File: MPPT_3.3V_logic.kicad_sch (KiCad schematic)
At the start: 28 parts, among them Q1 PMOS, Q11 PMOS, Q2 PMOS, U1 LTC4412xS6, U16 TPS259470ARPWR, U2 TPS62177DQCR, U3 LTC4412xS6, U5 LTC2965HDD-PBF

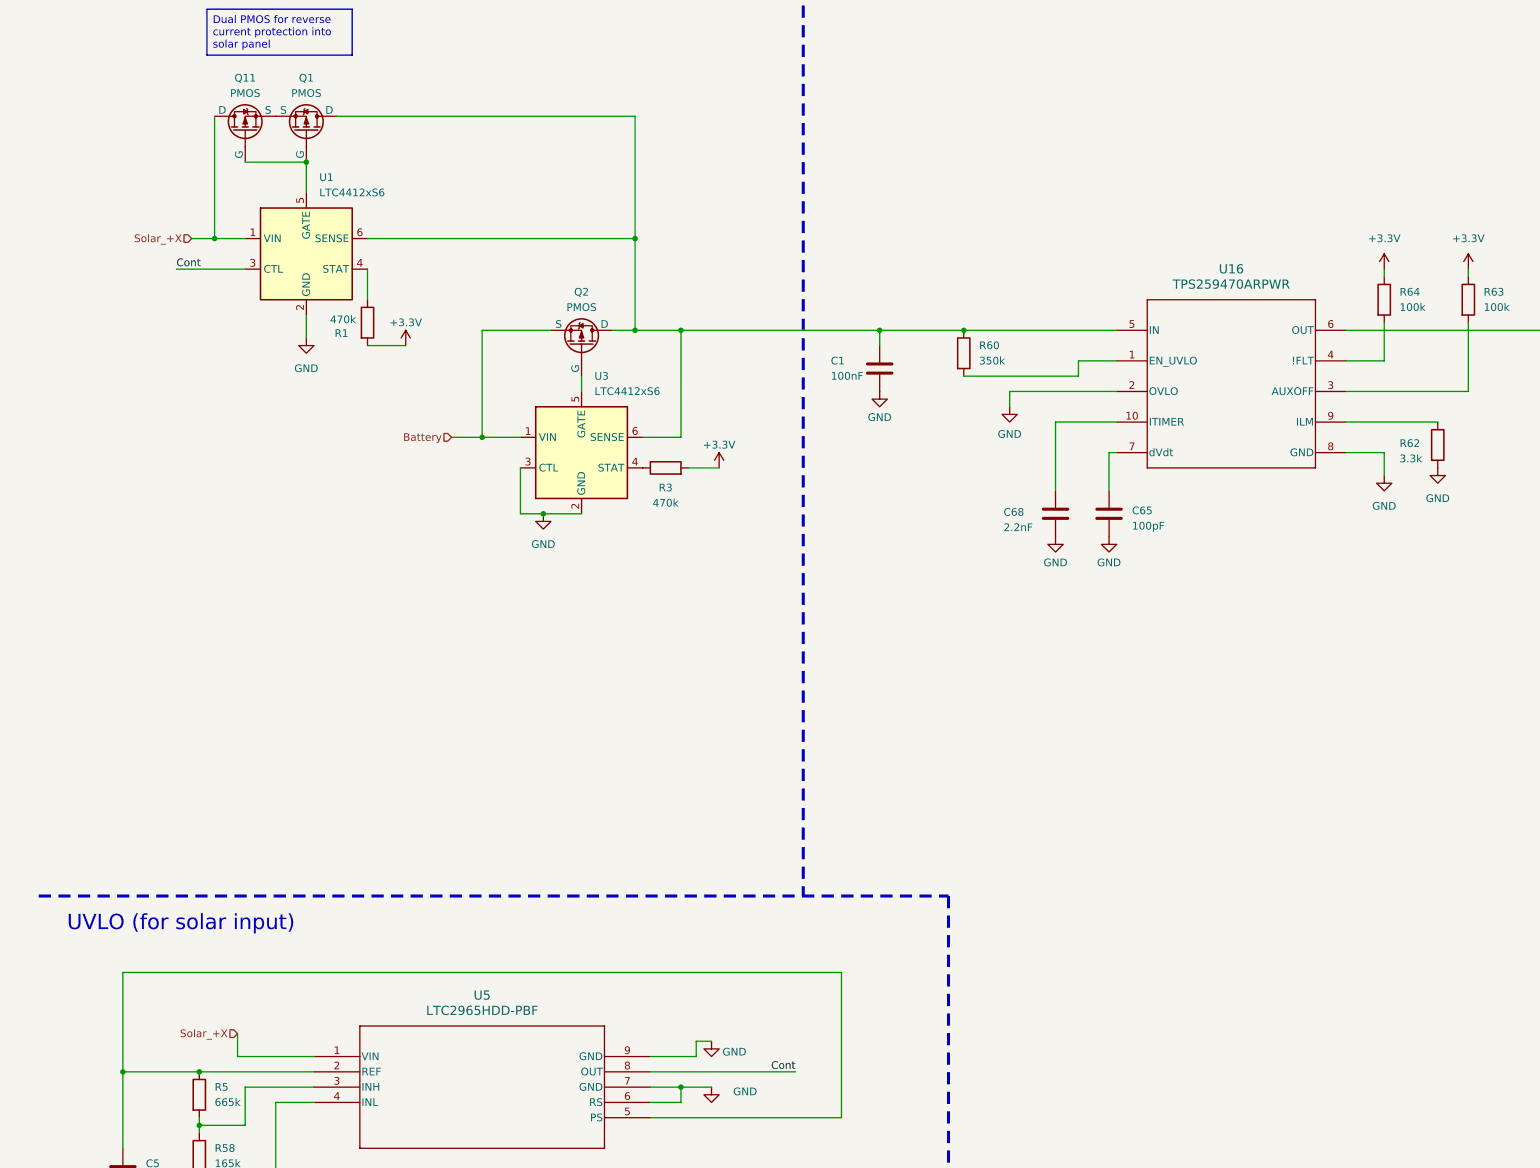
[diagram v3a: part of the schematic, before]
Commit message: added current sensing and e-fuses
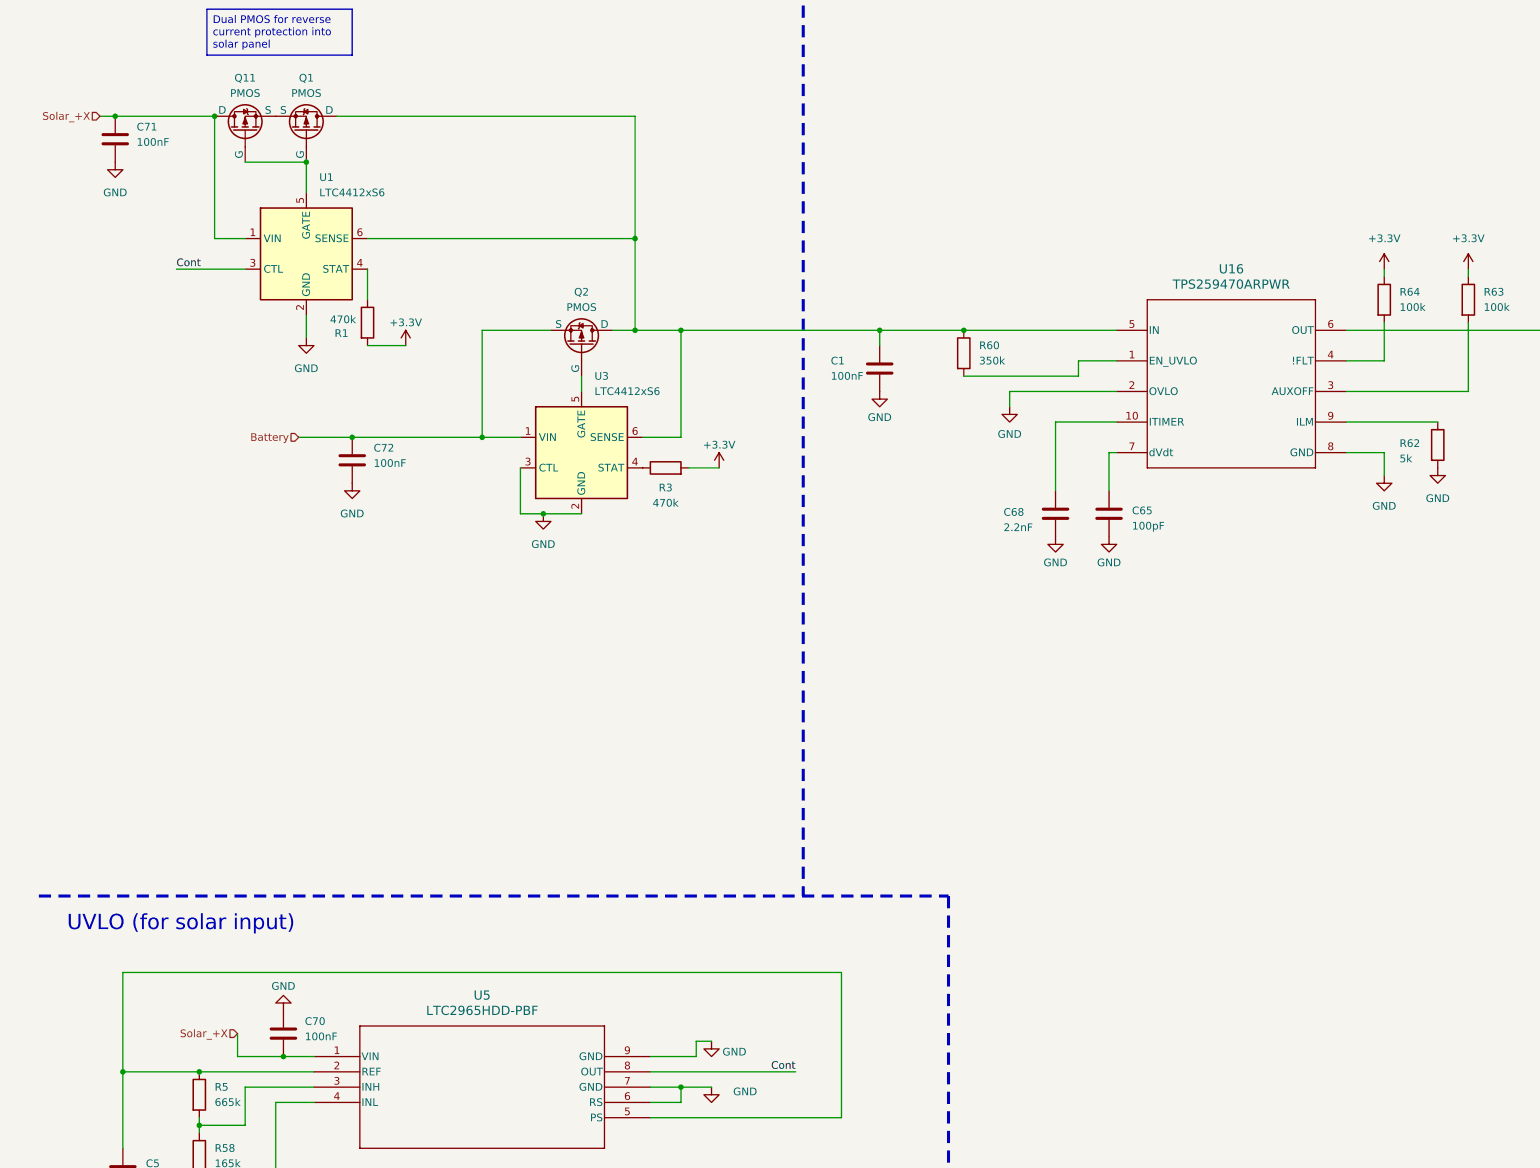
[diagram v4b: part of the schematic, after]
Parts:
- added C70, C71, C72: 100nF, Capacitor_SMD:C_1210_3225Metric, symbol Device:C
- R62: value 3.3k -> 5k
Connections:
- net Battery: now also C72.1
- net GND: now also C70.1, C71.2, C72.2
- net Solar_+X: now also C70.2, C71.1

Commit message: Added connectors to schematic
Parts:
- removed Q1, Q11, Q2: PMOS, symbol Simulation_SPICE:PMOS
- added Q15, Q16, Q17: SIR5607DP-T1-RE3, Package_SO:PowerPAK_SO-8_Single, symbol Transistor_FET:Si7141DP
- C1: renamed from C71; footprint Capacitor_SMD:C_1210_3225Metric -> Capacitor_SMD:C_0603_1608Metric; MANUFACTURER_PART_NUMBER CL32B226KAJNFNE -> 06035C104K4T2A
- C10: renamed from C65; footprint Capacitor_SMD:C_1210_3225Metric -> Capacitor_SMD:C_0603_1608Metric; MANUFACTURER_PART_NUMBER CL32B226KAJNFNE -> 885342206001
- C11: renamed from C70; footprint Capacitor_SMD:C_1210_3225Metric -> Capacitor_SMD:C_0603_1608Metric; MANUFACTURER_PART_NUMBER CL32B226KAJNFNE -> 06035C104K4T2A
- C12: renamed from C5; footprint Capacitor_SMD:C_1210_3225Metric -> Capacitor_SMD:C_0603_1608Metric; MANUFACTURER_PART_NUMBER CL32B226KAJNFNE -> C0603W102KDRACAUTO
- C2: renamed from C66; footprint Capacitor_SMD:C_1210_3225Metric -> Capacitor_SMD:C_0603_1608Metric; MANUFACTURER_PART_NUMBER CL32B226KAJNFNE -> CL10B105KQ8NNNC
- C3: renamed from C67; footprint Capacitor_SMD:C_1210_3225Metric -> zLibrary:CAP_C2220C_2S_KEM-M; MANUFACTURER_PART_NUMBER CL32B226KAJNFNE -> C2220C226MMR2L7289
- C4: renamed from C69; footprint Capacitor_SMD:C_1210_3225Metric -> Capacitor_SMD:C_0603_1608Metric; MANUFACTURER_PART_NUMBER CL32B226KAJNFNE -> 06035C104K4T2A
- C5: renamed from C1; footprint Capacitor_SMD:C_1210_3225Metric -> Capacitor_SMD:C_0603_1608Metric; MANUFACTURER_PART_NUMBER CL32B226KAJNFNE -> 06035C104K4T2A
- C6: renamed from C2; footprint Capacitor_SMD:C_0805_2012Metric -> zLibrary:CAP_C2220C_2S_KEM-M; MANUFACTURER_PART_NUMBER GRM21BZ71A226ME15L -> C2220C226MMR2L7289
- C7: renamed from C3; footprint Capacitor_SMD:C_0805_2012Metric -> zLibrary:CAP_C2220C_2S_KEM-M; MANUFACTURER_PART_NUMBER GRM21BZ71A226ME15L -> C2220C226MMR2L7289
- C8: renamed from C72; footprint Capacitor_SMD:C_1210_3225Metric -> Capacitor_SMD:C_0603_1608Metric; MANUFACTURER_PART_NUMBER CL32B226KAJNFNE -> 06035C104K4T2A
- C9: renamed from C68; footprint Capacitor_SMD:C_1210_3225Metric -> Capacitor_SMD:C_0603_1608Metric; MANUFACTURER_PART_NUMBER CL32B226KAJNFNE -> GCM1885C1H222FA16D
- L1: footprint (none) -> zLibrary:IND_BOURNS_SRR6038; MANUFACTURER (none) -> DigiKey; MANUFACTURER_PART_NUMBER (none) -> SRR6038-100Y
- R1: renamed from R64; footprint (none) -> Resistor_SMD:R_0603_1608Metric; MANUFACTURER (none) -> Digikey; MANUFACTURER_PART_NUMBER (none) -> AT0603FRE07100KL
- R10: renamed from R59; footprint (none) -> Resistor_SMD:R_0603_1608Metric; MANUFACTURER (none) -> Digikey; MANUFACTURER_PART_NUMBER (none) -> RN73R1JTTD4993F25
- R2: renamed from R63; footprint (none) -> Resistor_SMD:R_0603_1608Metric; MANUFACTURER (none) -> Digikey; MANUFACTURER_PART_NUMBER (none) -> AT0603FRE07100KL
- R3: renamed from R1; footprint (none) -> Resistor_SMD:R_0603_1608Metric; MANUFACTURER (none) -> Digikey; MANUFACTURER_PART_NUMBER (none) -> RN73R1JTTD4703F50
- R4: renamed from R60; footprint (none) -> Resistor_SMD:R_0603_1608Metric; MANUFACTURER (none) -> Digikey; MANUFACTURER_PART_NUMBER (none) -> RN73R1JTTD3483F25
- R5: renamed from R2; footprint (none) -> Resistor_SMD:R_0603_1608Metric; MANUFACTURER (none) -> Digikey; MANUFACTURER_PART_NUMBER (none) -> AT0603FRE07100KL
- R6: renamed from R62; footprint (none) -> Resistor_SMD:R_0603_1608Metric; MANUFACTURER (none) -> Digikey; MANUFACTURER_PART_NUMBER (none) -> RN73R1JTTD4991F100
- R7: renamed from R3; footprint (none) -> Resistor_SMD:R_0603_1608Metric; MANUFACTURER (none) -> Digikey; MANUFACTURER_PART_NUMBER (none) -> RN73R1JTTD4703F50
- R8: renamed from R5; footprint (none) -> Resistor_SMD:R_0603_1608Metric; MANUFACTURER (none) -> Digikey; MANUFACTURER_PART_NUMBER (none) -> RN73R1JTTD6653F25
- R9: renamed from R58; footprint (none) -> Resistor_SMD:R_0603_1608Metric; MANUFACTURER (none) -> Digikey; MANUFACTURER_PART_NUMBER (none) -> RN73R1JTTD1653F25
- U2: renamed from U16; footprint RPW0010A-MFG -> zLibrary:RPW0010A-MFG
- U3: renamed from U2; footprint DQC0010A -> zLibrary:DQC0010A
- renumbered U3 to U4
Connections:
- net +3.3V: now also U3.8 (SLEEP)
- net Battery: now also Q17.5 (D)
- net GND: no longer U3.8 (SLEEP)
- net Solar_+X: now also Q16.1 (S), Q16.2 (S), Q16.3 (S)
- net at C5.1, R4.1, U1.6 (SENSE)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: now also Q15.1 (S), Q15.2 (S), Q15.3 (S), Q17.1 (S), Q17.2 (S), Q17.3 (S)
- net at U1.5 (GATE): now also Q15.4 (G), Q16.4 (G)
- net at U4.5 (GATE): now also Q17.4 (G)
- new net: Q15.5 (D), Q16.5 (D)

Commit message: A bunch of misc schematic changes
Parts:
- renumbered Q16 to Q1, Q15 to Q2, Q17 to Q3
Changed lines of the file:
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@@
 		(on_board yes)
 		(dnp no)
-		(property "Reference" "#PWR012"
+		(property "Reference" "#PWR013"
 			(at 125.73 148.59 0)
 			(effects
@@
 			(project "EPS_mppt_board"
 				(path "/8f246f89-1ec7-4136-9977-839b50e116ed/1cb04f15-5cd4-4c9d-a391-62735eda9253"
-					(reference "#PWR012")
+					(reference "#PWR013")
 					(unit 1)
 				)
@@
 		(on_board yes)
 		(dnp no)
-		(property "Reference" "#PWR017"
+		(property "Reference" "#PWR018"
 			(at 181.61 162.56 0)
 			(effects
@@
 			(project "EPS_mppt_board"
 				(path "/8f246f89-1ec7-4136-9977-839b50e116ed/1cb04f15-5cd4-4c9d-a391-62735eda9253"
-					(reference "#PWR017")
+					(reference "#PWR018")
 					(unit 1)
 				)
@@
 					(size 1.27 1.27)
 				)
+				(hide yes)
 			)
 		)
@@
 					(size 1.27 1.27)
 				)
+				(hide yes)
 			)
 		)
@@
 					(size 1.27 1.27)
 				)
+				(hide yes)
 			)
 		)
@@
 					(size 1.27 1.27)
 				)
+				(hide yes)
 			)
 		)
@@
 					(size 1.27 1.27)
 				)
+				(hide yes)
 			)
 		)
@@
 					(size 1.27 1.27)
 				)
+				(hide yes)
 			)
 		)
@@
 		(on_board yes)
 		(dnp no)
-		(property "Reference" "#PWR021"
+		(property "Reference" "#PWR022"
 			(at 124.46 246.38 0)
 			(effects
@@
 			(project "EPS_mppt_board"
 				(path "/8f246f89-1ec7-4136-9977-839b50e116ed/1cb04f15-5cd4-4c9d-a391-62735eda9253"
-					(reference "#PWR021")
+					(reference "#PWR022")
 					(unit 1)
 				)
@@
 		(dnp no)
 		(fields_autoplaced yes)
-		(property "Reference" "#PWR023"
+		(property "Reference" "#PWR024"
 			(at 39.37 284.48 0)
 			(effects
@@
 			(project "EPS_mppt_board"
 				(path "/8f246f89-1ec7-4136-9977-839b50e116ed/1cb04f15-5cd4-4c9d-a391-62735eda9253"
-					(reference "#PWR023")
+					(reference "#PWR024")
 					(unit 1)
 				)
@@
 					(size 1.27 1.27)
 				)
+				(hide yes)
 			)
 		)
@@
 					(size 1.27 1.27)
 				)
+				(hide yes)
 			)
 		)
@@
 		(dnp no)
 		(fields_autoplaced yes)
-		(property "Reference" "#PWR013"
+		(property "Reference" "#PWR014"
 			(at 245.11 151.13 0)
 			(effects
@@
 			(project "EPS_mppt_board"
 				(path "/8f246f89-1ec7-4136-9977-839b50e116ed/1cb04f15-5cd4-4c9d-a391-62735eda9253"
-					(reference "#PWR013")
+					(reference "#PWR014")
 					(unit 1)
 				)
@@
 		(on_board yes)
 		(dnp no)
-		(property "Reference" "Q16"
+		(property "Reference" "Q1"
 			(at 38.862 79.756 90)
 			(effects
@@
 			(project "EPS_mppt_board"
 				(path "/8f246f89-1ec7-4136-9977-839b50e116ed/1cb04f15-5cd4-4c9d-a391-62735eda9253"
-					(reference "Q16")
+					(reference "Q1")
 					(unit 1)
 				)
@@
 		(dnp no)
 		(fields_autoplaced yes)
-		(property "Reference" "#PWR015"
+		(property "Reference" "#PWR016"
 			(at 64.77 153.67 0)
 			(effects
@@
 			(project "EPS_mppt_board"
 				(path "/8f246f89-1ec7-4136-9977-839b50e116ed/1cb04f15-5cd4-4c9d-a391-62735eda9253"
-					(reference "#PWR015")
+					(reference "#PWR016")
 					(unit 1)
 				)
@@
 					(size 1.27 1.27)
 				)
+				(hide yes)
 			)
 		)
@@
 					(size 1.27 1.27)
 				)
+				(hide yes)
 			)
 		)
@@
 		(on_board yes)
 		(dnp no)
-		(property "Reference" "#PWR020"
+		(property "Reference" "#PWR021"
 			(at 53.34 228.6 0)
 			(effects
@@
 			(project "EPS_mppt_board"
 				(path "/8f246f89-1ec7-4136-9977-839b50e116ed/1cb04f15-5cd4-4c9d-a391-62735eda9253"
-					(reference "#PWR020")
+					(reference "#PWR021")
 					(unit 1)
 				)
@@
 		(dnp no)
 		(fields_autoplaced yes)
-		(property "Reference" "#PWR016"
+		(property "Reference" "#PWR017"
 			(at 96.52 158.75 0)
 			(effects
@@
 			(project ""
 				(path "/8f246f89-1ec7-4136-9977-839b50e116ed/1cb04f15-5cd4-4c9d-a391-62735eda9253"
-					(reference "#PWR016")
+					(reference "#PWR017")
 					(unit 1)
 				)
@@
 					(size 1.27 1.27)
 				)
+				(hide yes)
 			)
 		)
@@
 					(size 1.27 1.27)
 				)
+				(hide yes)
 			)
 		)
@@
 					(size 1.27 1.27)
 				)
+				(hide yes)
 			)
 		)
@@
 					(size 1.27 1.27)
 				)
+				(hide yes)
 			)
 		)
@@
 		(on_board yes)
 		(dnp no)
-		(property "Reference" "Q15"
+		(property "Reference" "Q2"
 			(at 65.024 80.01 90)
 			(effects
@@
 			(project ""
 				(path "/8f246f89-1ec7-4136-9977-839b50e116ed/1cb04f15-5cd4-4c9d-a391-62735eda9253"
-					(reference "Q15")
+					(reference "Q2")
 					(unit 1)
 				)
@@
 		(dnp no)
 		(fields_autoplaced yes)
-		(property "Reference" "#PWR019"
+		(property "Reference" "#PWR020"
 			(at 342.9 168.91 0)
 			(effects
@@
 			(project ""
 				(path "/8f246f89-1ec7-4136-9977-839b50e116ed/1cb04f15-5cd4-4c9d-a391-62735eda9253"
-					(reference "#PWR019")
+					(reference "#PWR020")
 					(unit 1)
 				)
@@
 					(size 1.27 1.27)
 				)
+				(hide yes)
 			)
 		)
@@
 					(size 1.27 1.27)
 				)
+				(hide yes)
 			)
 		)
@@
 					(size 1.27 1.27)
 				)
+				(hide yes)
 			)
 		)
@@
 					(size 1.27 1.27)
 				)
+				(hide yes)
 			)
 		)
@@
 		(on_board yes)
 		(dnp no)
-		(property "Reference" "#PWR022"
+		(property "Reference" "#PWR023"
 			(at 124.46 254 0)
 			(effects
@@
 			(project "EPS_mppt_board"
 				(path "/8f246f89-1ec7-4136-9977-839b50e116ed/1cb04f15-5cd4-4c9d-a391-62735eda9253"
-					(reference "#PWR022")
+					(reference "#PWR023")
 					(unit 1)
 				)
@@
 					(size 1.27 1.27)
 				)
+				(hide yes)
 			)
 		)
@@
 					(size 1.27 1.27)
 				)
+				(hide yes)
 			)
 		)
@@
 					(size 1.27 1.27)
 				)
+				(hide yes)
 			)
 		)
@@
 					(size 1.27 1.27)
 				)
+				(hide yes)
 			)
 		)
@@
 		(on_board yes)
 		(dnp no)
-		(property "Reference" "#PWR0165"
+		(property "Reference" "#PWR012"
 			(at 307.34 138.43 0)
 			(effects
@@
 			(project "EPS_mppt_board"
 				(path "/8f246f89-1ec7-4136-9977-839b50e116ed/1cb04f15-5cd4-4c9d-a391-62735eda9253"
-					(reference "#PWR0165")
+					(reference "#PWR012")
 					(unit 1)
 				)
@@
 		(dnp no)
 		(fields_autoplaced yes)
-		(property "Reference" "#PWR014"
+		(property "Reference" "#PWR015"
 			(at 236.22 152.4 0)
 			(effects
@@
 			(project "EPS_mppt_board"
 				(path "/8f246f89-1ec7-4136-9977-839b50e116ed/1cb04f15-5cd4-4c9d-a391-62735eda9253"
-					(reference "#PWR014")
+					(reference "#PWR015")
 					(unit 1)
 				)
@@
 		(dnp no)
 		(fields_autoplaced yes)
-		(property "Reference" "Q17"
+		(property "Reference" "Q3"
 			(at 102.87 115.57 90)
 			(effects
@@
 			(project "EPS_mppt_board"
 				(path "/8f246f89-1ec7-4136-9977-839b50e116ed/1cb04f15-5cd4-4c9d-a391-62735eda9253"
-					(reference "Q17")
+					(reference "Q3")
 					(unit 1)
 				)
@@
 		(on_board yes)
 		(dnp no)
-		(property "Reference" "#PWR018"
+		(property "Reference" "#PWR019"
 			(at 190.5 162.56 0)
 			(effects
@@
 			(project "EPS_mppt_board"
 				(path "/8f246f89-1ec7-4136-9977-839b50e116ed/1cb04f15-5cd4-4c9d-a391-62735eda9253"
-					(reference "#PWR018")
+					(reference "#PWR019")
 					(unit 1)
 				)

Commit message: Changed LTC 4412 to 4417, still kinks to work out
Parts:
- removed C11, C8: 100nF, Capacitor_SMD:C_0603_1608Metric, symbol Device:C
- removed C12: 1nF, Capacitor_SMD:C_0603_1608Metric, symbol Device:C
- removed U1, U4: LTC4412xS6, Package_TO_SOT_SMD:TSOT-23-6, symbol Power_Management:LTC4412xS6
- removed U5: LTC2965HDD-PBF, IC's_Sat:DFN-8_DD_LIT, symbol LTC2965HDD#PBF:LTC2965HDD-PBF
- added C2, C3: 100nF, Capacitor_SMD:C_0603_1608Metric, symbol Device:C
- added C4: 1uF, Capacitor_SMD:C_0603_1608Metric, symbol Device:C
- added C5: 6.8nF, Capacitor_SMD:C_0603_1608Metric, symbol Device:C
- added C6: 100uF, Capacitor_Tantalum_SMD:CP_EIA-7361-38_AVX-V, symbol Device:C
- added D1: BAT54J, Diode_SMD:D_SOD-323F, symbol Diode:BAT54J
- added Q4: SIR5607DP-T1-RE3, Package_SO:PowerPAK_SO-8_Single, symbol Transistor_FET:Si7141DP
- added R1, R4: 1M, Resistor_SMD:R_0603_1608Metric, symbol Device:R
- added R11, R12, R13: 100k, Resistor_SMD:R_0603_1608Metric, symbol Device:R
- added R2: 140k, Resistor_SMD:R_0603_1608Metric, symbol Device:R
- added R5: 57.6k, Resistor_SMD:R_0603_1608Metric, symbol Device:R
- added R6: 52.3k, Resistor_SMD:R_0603_1608Metric, symbol Device:R
- added U1: LTC4417HUF, Package_DFN_QFN:QFN-24-1EP_4x4mm_P0.5mm_EP2.6x2.6mm, symbol Power_Management:LTC4417HUF
- Q1, Q2, Q3: MANUFACTURER_PART_NUMBER (none) -> SIR5607DP-T1-RE3
- R10: value 499k -> 2.21k; MANUFACTURER Digikey -> (none); MANUFACTURER_PART_NUMBER RN73R1JTTD4993F25 -> RMCF0603FT2K21
- R3: value 470k -> 60.4k; MANUFACTURER Digikey -> (none); MANUFACTURER_PART_NUMBER RN73R1JTTD4703F50 -> RT0603FRE0760K4L
- R7: value 470k -> 1M; MANUFACTURER Digikey -> (none); MANUFACTURER_PART_NUMBER RN73R1JTTD4703F50 -> CPF0603B1M0E
- R8: value 665k -> 82.5k; MANUFACTURER Digikey -> (none); MANUFACTURER_PART_NUMBER RN73R1JTTD6653F25 -> ERA-3AEB8252V
- R9: value 165k -> 412k; MANUFACTURER Digikey -> (none); MANUFACTURER_PART_NUMBER RN73R1JTTD1653F25 -> RT0603BRD07412KL
- renumbered C2 to C10, C3 to C11, C4 to C12, C6 to C13, C7 to C14, C5 to C7, C9 to C8, C10 to C9, R4 to R14, R1 to R15, R6 to R16, R2 to R17, R5 to R18
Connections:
- net +3.3V: now also R7.1, C2.1, R11.1, R12.1, R13.1, U1.14 (VS3), U1.19 (V3); no longer R3.2, R7.2
- net Battery: now also C1.1, Q2.5 (D), R1.1, U1.21 (V1); no longer Q3.5 (D)
- net GND: now also R3.2, R9.2, C2.2, C3.2, C4.2, C6.2, R6.2, U1.10 (GND), U1.24 (HYS), U1.25 (PAD); no longer R10.2
- net Solar_+X: now also Q3.5 (D), C3.1, R4.1, U1.16 (VS2), U1.20 (V2); no longer C1.1, Q1.1 (S), Q1.2 (S), Q1.3 (S)
- net at R10.1: now also D1.2 (A), U1.17 (G1); no longer R9.2
- net at Q3.4 (G): now also Q4.4 (G), U1.15 (G2)
- net at Q1.4 (G), Q2.4 (G): now also R10.2, C5.1, D1.1 (K)
- net at Q1.5 (D): now also C7.1, R14.1, U2.5 (IN), C5.2, C6.1, Q4.5 (D), U1.12 (VOUT); no longer Q2.5 (D)
- net UV3: now reaches R8.1
- net UV3: now also R7.2, U1.5 (UV3)
- net OV3: now reaches R8.2, R9.1
- net OV3: now also U1.6 (OV3)
- net OV1: now reaches R3.1
- net OV1: now also R2.2, U1.2 (OV1)
- new net: C4.1, Q1.1 (S), Q1.2 (S), Q1.3 (S), Q2.1 (S), Q2.2 (S), Q2.3 (S), U1.18 (VS1)
- new net: Q3.1 (S), Q3.2 (S), Q3.3 (S), Q4.1 (S), Q4.2 (S), Q4.3 (S)
- new net !VAL1: R11.2, U1.7 (~{VALID1})
- new net !VAL2: R12.2, U1.8 (~{VALID2})
- new net !VAL3: R13.2, U1.9 (~{VALID3})
- new net OV2: R5.2, R6.1, U1.4 (OV2)
- new net UV1: R1.2, R2.1, U1.1 (UV1)
- new net UV2: R4.2, R5.1, U1.3 (UV2)
- no-connect marks 0 -> 4
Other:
- note removed: "UVLO (for solar input)"
- moved on the sheet: C10, C11, C12, C13, C14, C7, C8, C9, L1, R14, R15, R16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
